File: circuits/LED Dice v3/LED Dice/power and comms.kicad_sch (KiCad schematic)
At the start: 25 parts, among them J1 KH-TYPE-C-16P, J3 Conn_01x02_Pin, U3 TP4057, U4 LTST-C195KGJRKT, U5 TLV74333PDBVR, U6 MT3608

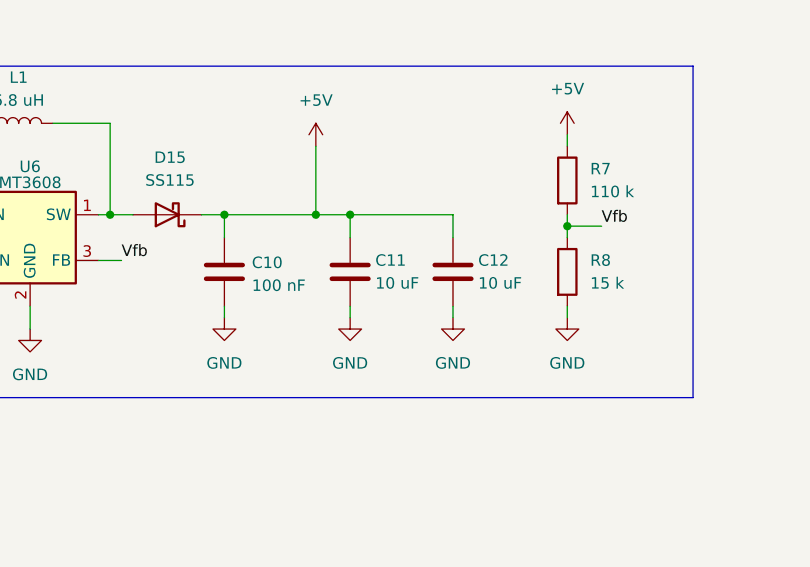
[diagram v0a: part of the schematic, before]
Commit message: added BOM
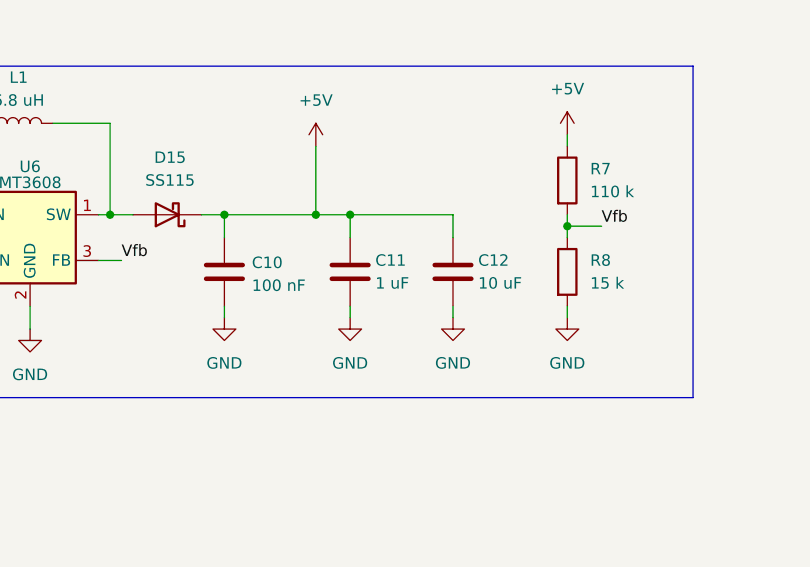
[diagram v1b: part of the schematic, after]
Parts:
- C11: value 10 uF -> 1 uF; Part No CL31A106KAHNNNE -> CL21B105KBFNNNE
- R1: footprint Resistor_SMD:R_0603_1608Metric -> Resistor_SMD:R_0603_1608Metric_Pad0.98x0.95mm_HandSolder
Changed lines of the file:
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@@
 			)
 		)
-		(property "Value" "10 uF"
+		(property "Value" "1 uF"
 			(at 237.744 133.35 0)
 			(show_name no)
@@
 			)
 		)
-		(property "Part No" "CL31A106KAHNNNE"
+		(property "Part No" "CL21B105KBFNNNE"
 			(at 234.95 132.08 0)
 			(hide yes)
@@
 			)
 		)
-		(property "Footprint" "Resistor_SMD:R_0603_1608Metric"
+		(property "Footprint" "Resistor_SMD:R_0603_1608Metric_Pad0.98x0.95mm_HandSolder"
 			(at 102.108 43.18 90)
 			(hide yes)
